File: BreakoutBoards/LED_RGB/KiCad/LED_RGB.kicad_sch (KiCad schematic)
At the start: 5 parts, among them J1 HDR-TH_4P-P2.54-V-M

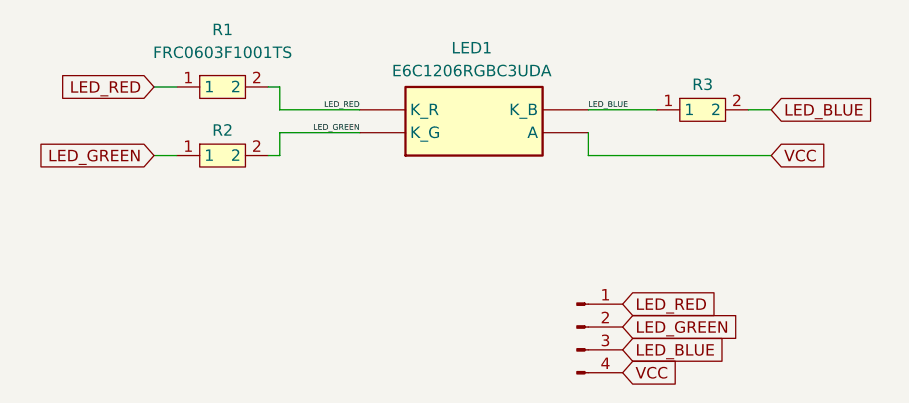
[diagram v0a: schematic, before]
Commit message: removing resistors to make more versatile and selecting new led to use
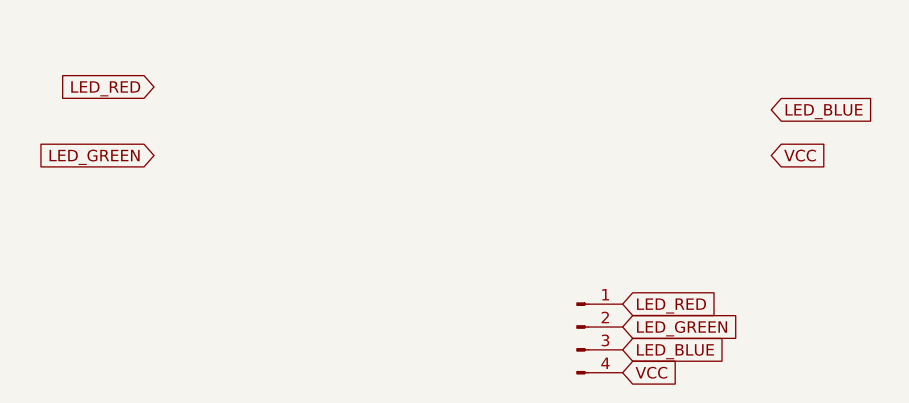
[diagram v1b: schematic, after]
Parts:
- removed LED1: E6C1206RGBC3UDA, clectric-diy:E6C1206RGBC3UDA, symbol clectric-diy:E6C1206RGBC3UDA
- removed R1, R2, R3: FRC0603F1001TS, clectric-diy:R0603, symbol clectric-diy:FRC0603F1001TS
- J1: value HDR-TH_4P-P2.54-V-M -> ~; footprint clectric-diy:HDR-TH_4P-P2.54-V-M -> Connector_PinHeader_2.54mm:PinHeader_1x04_P2.54mm_Vertical
